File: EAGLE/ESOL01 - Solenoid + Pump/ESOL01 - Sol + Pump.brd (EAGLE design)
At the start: 7 parts, among them J1 ECAM02, J2 SOL1, J3 SOL2, J4 SOL3, J5 SOL4, J6 PUMP

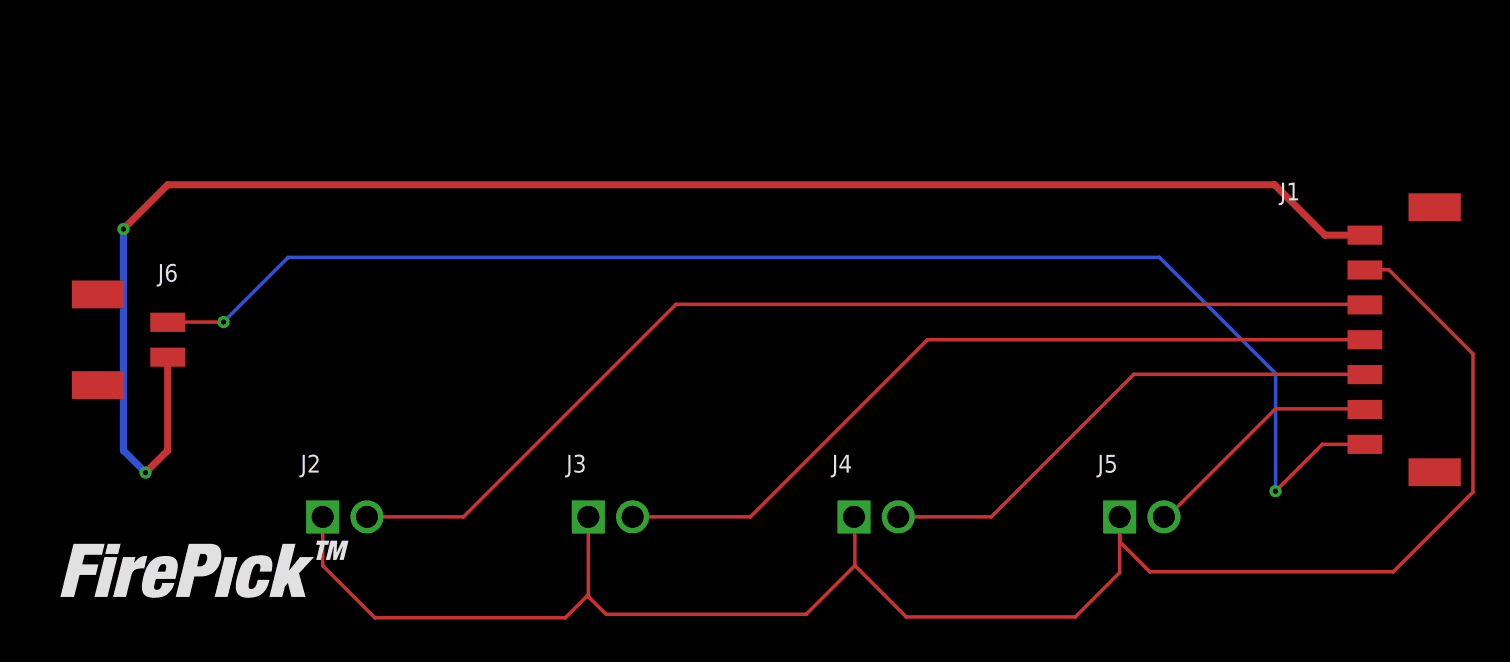
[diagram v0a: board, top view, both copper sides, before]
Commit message: Routed ESOL01, created MTHOLE(M3) part for future use
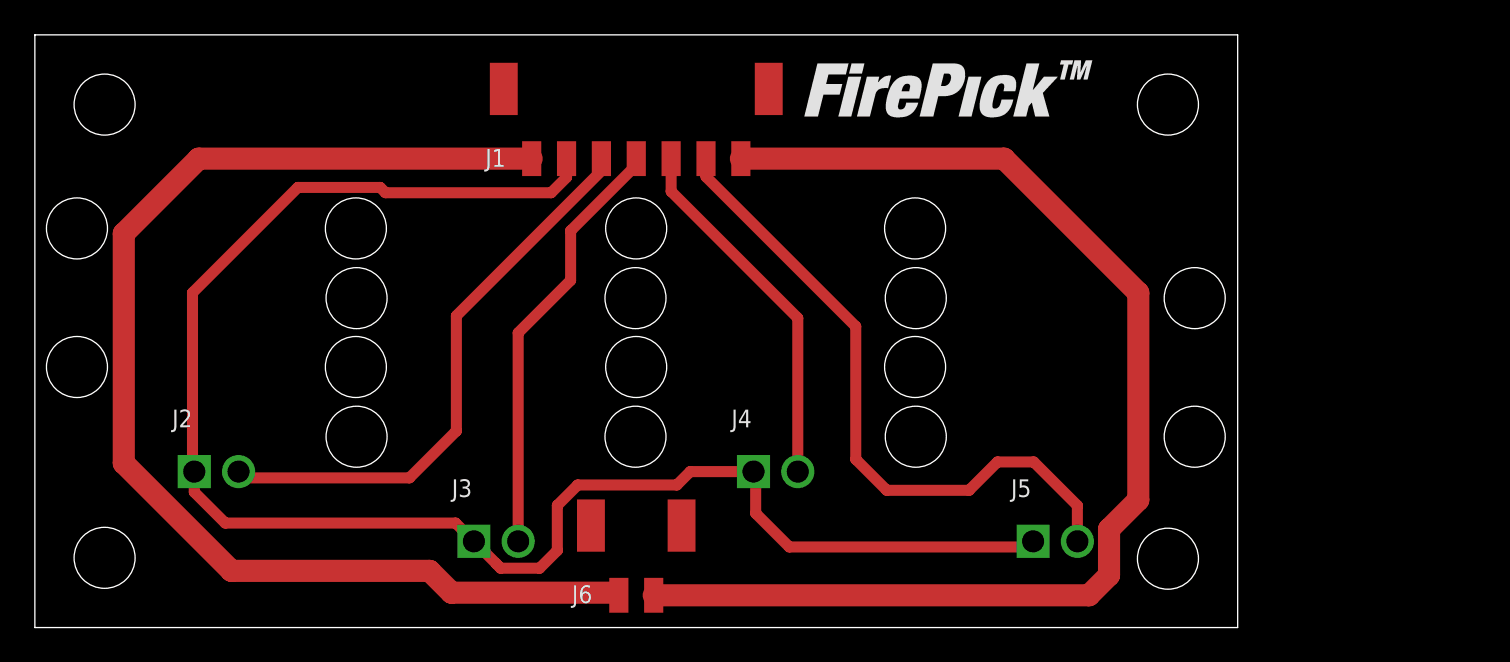
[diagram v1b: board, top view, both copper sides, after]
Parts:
- added MT1: : (5MM, 5MM), TinWhiskers:MTHOLE(M3)
- added MT2: : (5MM, 29MM), TinWhiskers:MTHOLE(M3)
- added MT3: : (64MM, 29MM), TinWhiskers:MTHOLE(M3)
- added MT4: : (64MM, 5MM), TinWhiskers:MTHOLE(M3)
- moved LOGO2 50.8 mm to (43.9, 27.6)
- moved J1 43.0 mm to (34.5, 26.8), turned to 0 degrees
- moved J6 30.6 mm to (34.5, 1.85), turned to 0 degrees
- moved J2 7.81 mm to (10.4, 8.95)
- moved J3 6.71 mm to (26.5, 4.95)
- moved J4 6.32 mm to (42.5, 8.95)
- moved J5 5.16 mm to (58.5, 4.95)
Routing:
- net N$7: track 62.3 -> 32.8 mm
- net +24V: track 95.1 -> 69.9 mm, vias 2 -> 0
- net N$10: track 14.1 -> 38.0 mm
- net N$8: track 46.2 -> 24.8 mm
- net N$11: track 80.8 -> 69.5 mm, vias 2 -> 0
- net +5V: track 105.2 -> 94.1 mm
- net N$9: track 30.2 -> 21.0 mm
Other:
- board outline added: 69 x 34 mm

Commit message: Fixed ESOL01 for mechanical restrictions
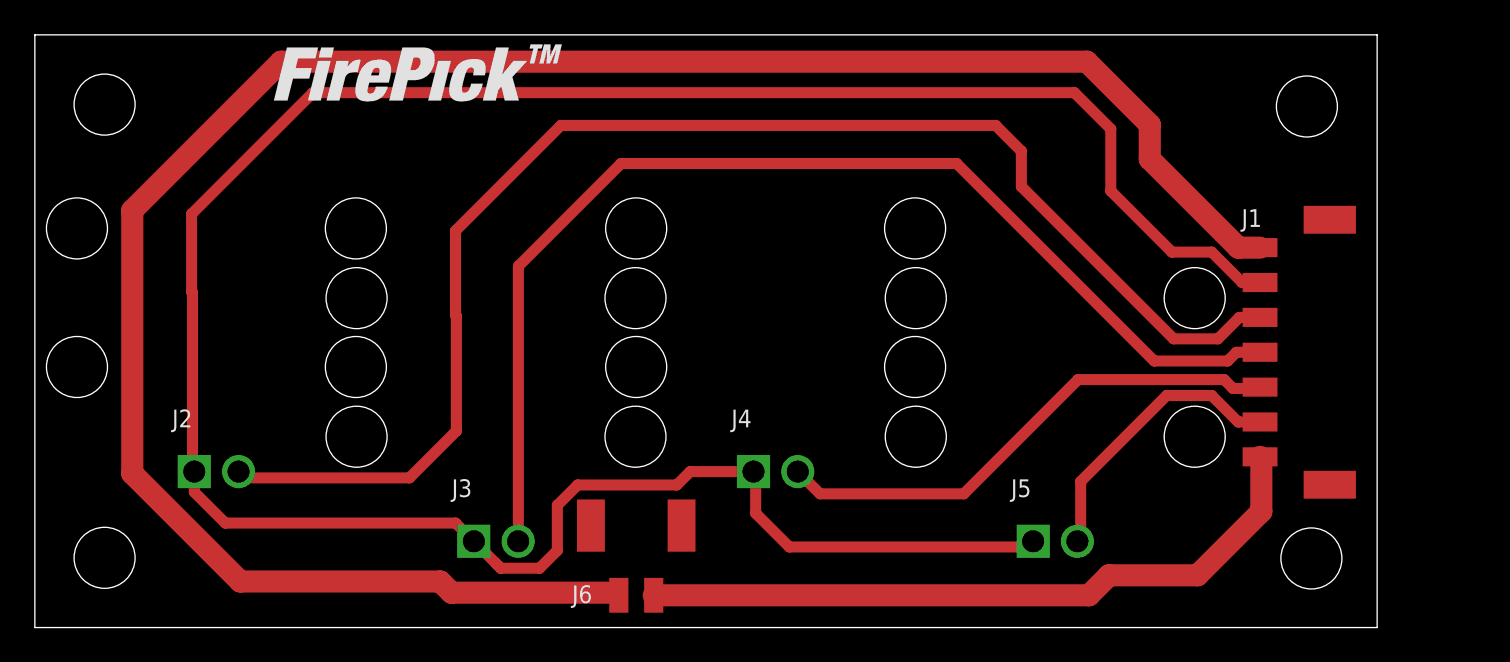
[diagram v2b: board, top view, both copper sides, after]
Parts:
- moved J1 37.3 mm to (70.2, 15.8), turned to 270 degrees
- moved LOGO2 30.4 mm to (13.5, 28.5)
- moved MT4 8.23 mm to (73.2, 3.96)
- moved MT3 7.97 mm to (73.0, 29.9)
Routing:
- net +24V: track 69.9 -> 119.7 mm
- net +5V: track 94.1 -> 143.8 mm
- net N$7: track 32.8 -> 80.7 mm
- net N$8: track 24.8 -> 65.7 mm
- net N$11: track 69.5 -> 40.0 mm
- net N$10: track 38.0 -> 16.5 mm
- net N$9: track 21.0 -> 30.0 mm
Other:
- board size 69 x 34 mm -> 77 x 34 mm

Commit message: Made REV 2 modifications, including increasing width of power traces, adding vias to power traces, and addition of LEDs to all modular tools. Catch diodes added to ESOL01 board to prevent coils from creating problems "upstream"
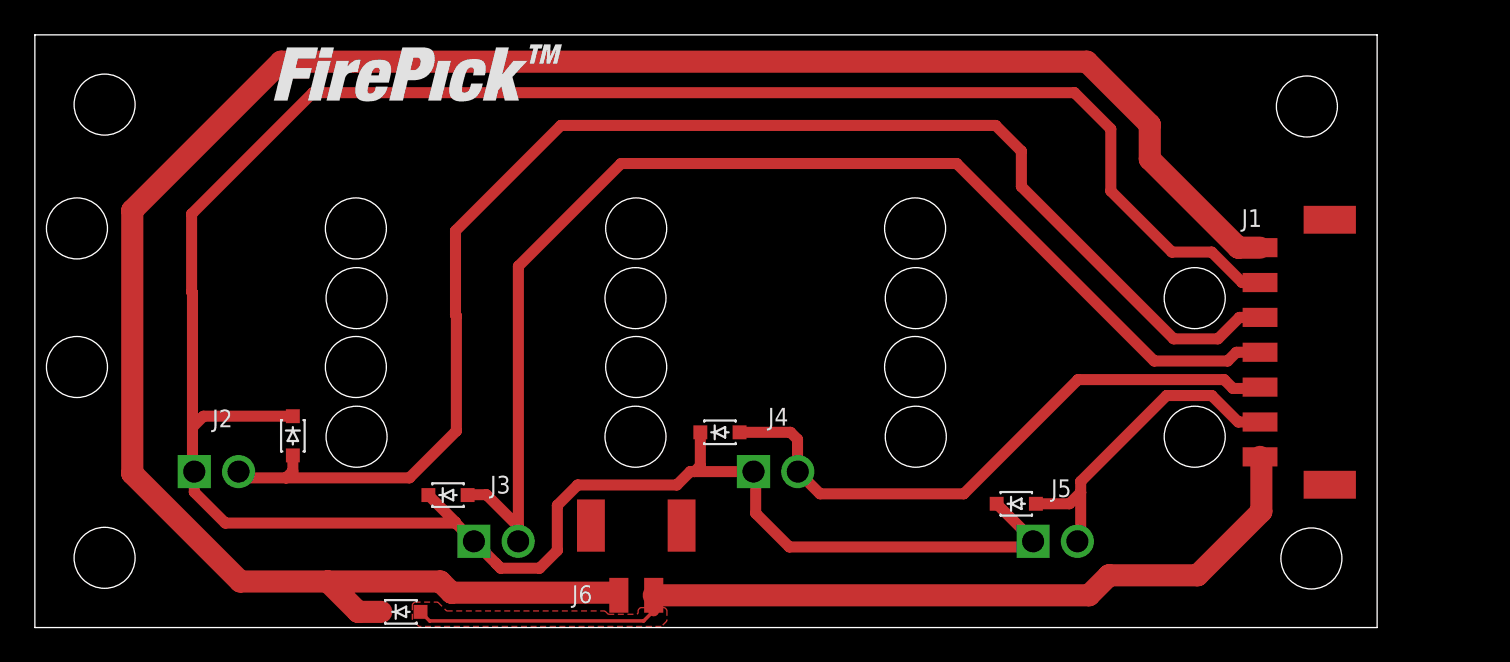
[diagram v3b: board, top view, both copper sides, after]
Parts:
- added D1, D2, D3, D4, D5: 1N4148, TinWhiskers:SOD-323
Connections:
- net +24V: now also D5.NEG
- net +5V: now also D1.NEG, D2.NEG, D3.NEG, D4.NEG
- net N$10: now also D4.POS
- net N$11: now also D5.POS
- net N$7: now also D1.POS
- net N$8: now also D2.POS
- net N$9: now also D3.POS
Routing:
- net N$11: track 40.0 -> 54.7 mm
- net +5V: track 143.8 -> 157.5 mm
- net N$9: track 30.0 -> 35.4 mm
- net +24V: track 119.7 -> 123.5 mm
- net N$8: track 65.7 -> 69.3 mm
- net N$10: track 16.5 -> 19.3 mm
- net N$7: track 80.7 -> 82.1 mm
- added copper zone on layer 1, net N$11
